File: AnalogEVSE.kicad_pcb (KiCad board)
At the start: 2 copper layers, 84.7 x 66 mm, 72 parts, among them K1 Relay, P1 230V, P2 Relay 2, P3 Relay 1, P4 Pilot, P5 Status LEDs, P6 Rext, P7 Power, Q1 BC337, Q2 BC557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

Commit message: Cleanup
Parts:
- C3: value 220n -> 1u
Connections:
- U5 pad 12: -12V -> Net-(U5-Pad12)
- U5 pad 3: +12V -> Net-(U5-Pad3)
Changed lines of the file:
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@@
     (zones 0)
     (modules 72)
-    (nets 52)
+    (nets 54)
   )
   (page A4)
@@
   (net 50 "Net-(U4-Pad9)")
   (net 51 "Net-(U4-Pad13)")
+  (net 52 "Net-(U5-Pad3)")
+  (net 53 "Net-(U5-Pad12)")
   (net_class Default "This is the default net class."
     (clearance 0.1)
@@
     (add_net "Net-(U4-Pad7)")
     (add_net "Net-(U4-Pad9)")
+    (add_net "Net-(U5-Pad12)")
+    (add_net "Net-(U5-Pad3)")
     (add_net Vcharge)
     (add_net Vconn)
@@
       (effects (font (size 1.016 1.016) (thickness 0.2032)))
     )
-    (fp_text value 220n (at 0 0 180) (layer F.SilkS) hide
+    (fp_text value 1u (at 0 0 180) (layer F.SilkS) hide
       (effects (font (size 1.016 1.016) (thickness 0.2032)))
     )
@@
       (net 38 "Net-(R10-Pad1)"))
     (pad 3 thru_hole oval (at -2.54 3.81 270) (size 1.5 2.286) (drill 0.8) (layers *.Cu *.Mask F.SilkS)
-      (net 1 +12V))
+      (net 52 "Net-(U5-Pad3)"))
     (pad 4 thru_hole oval (at 0 3.81 270) (size 1.5 2.286) (drill 0.8) (layers *.Cu *.Mask F.SilkS)
       (net 24 "Net-(C11-Pad1)"))
@@
       (net 38 "Net-(R10-Pad1)"))
     (pad 12 thru_hole oval (at -2.54 -3.81 270) (size 1.5 2.286) (drill 0.8) (layers *.Cu *.Mask F.SilkS)
-      (net 2 -12V))
+      (net 53 "Net-(U5-Pad12)"))
     (pad 13 thru_hole oval (at -5.08 -3.81 270) (size 1.5 2.286) (drill 0.8) (layers *.Cu *.Mask F.SilkS)
       (net 39 "Net-(R15-Pad1)"))

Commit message: Release 2.0.3
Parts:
- removed the ? at (137.5, 73.3)
- removed the ? at (137.5, 77.7)
- removed the ? at (164.6, 66.9)
- removed the ? at (164.6, 72.0)
- moved D3 1.42 mm to (176.0, 53.5), turned to 0 degrees
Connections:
- K1 pad 8: +12V -> Net-(C6-Pad2)
- K1 pad 9: Net-(C6-Pad2) -> +12V
- U5 pad 12: Net-(U5-Pad12) -> -12V
- U5 pad 3: Net-(U5-Pad3) -> +12V
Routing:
- net +12V: track 285.6 -> 271.3 mm, vias 4 -> 2
- net Net-(D11-Pad2): track 83.7 -> 69.8 mm
- net Net-(D11-Pad1): track 37.2 -> 50.0 mm
- net Net-(D6-Pad1): track 142.1 -> 143.5 mm
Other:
- net class Power: via_dia 1.4 -> 1.6; via_drill 0.6 -> 0.8
- board text added: "www.analogevse.xyz v2.0.3 12/2019"
- board text removed: "www.analogevse.xyz v2.0.0 01/2019"

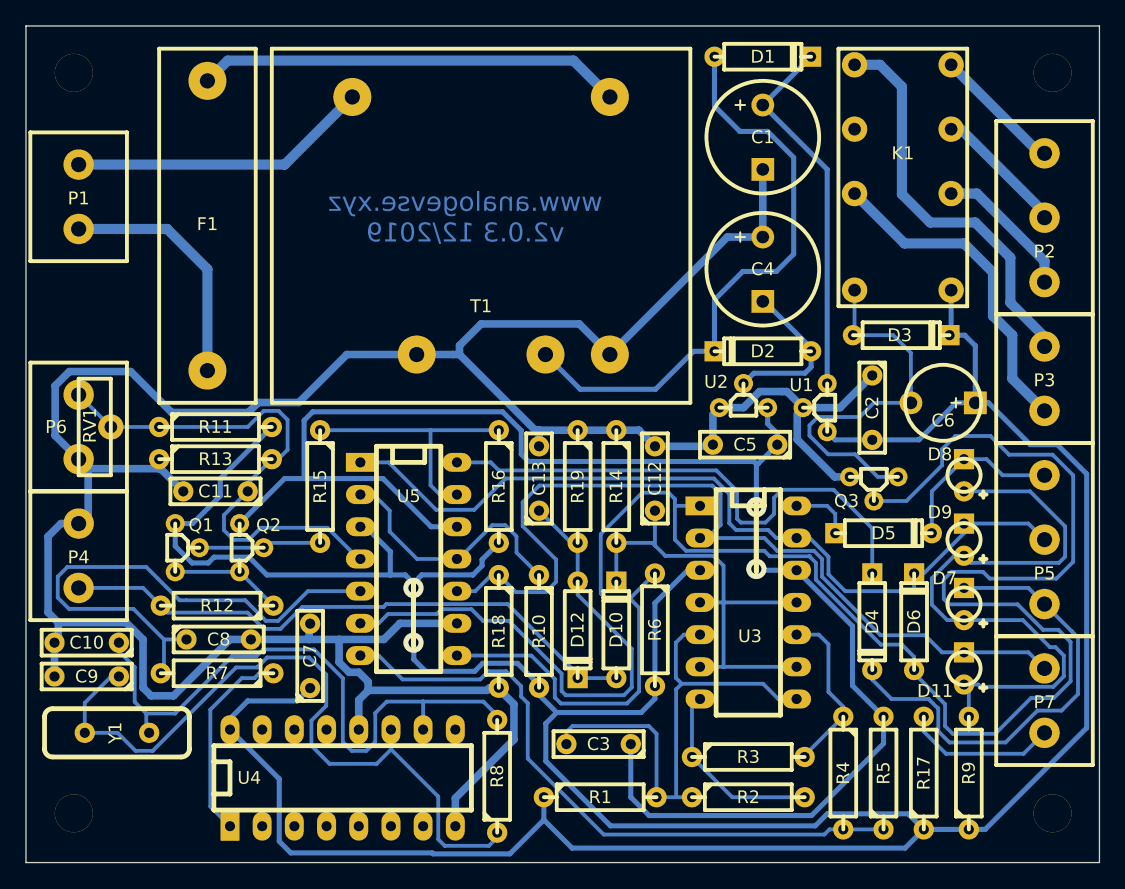
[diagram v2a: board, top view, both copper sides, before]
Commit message: Version 2.0.4 with R20 for proper +12V when idle
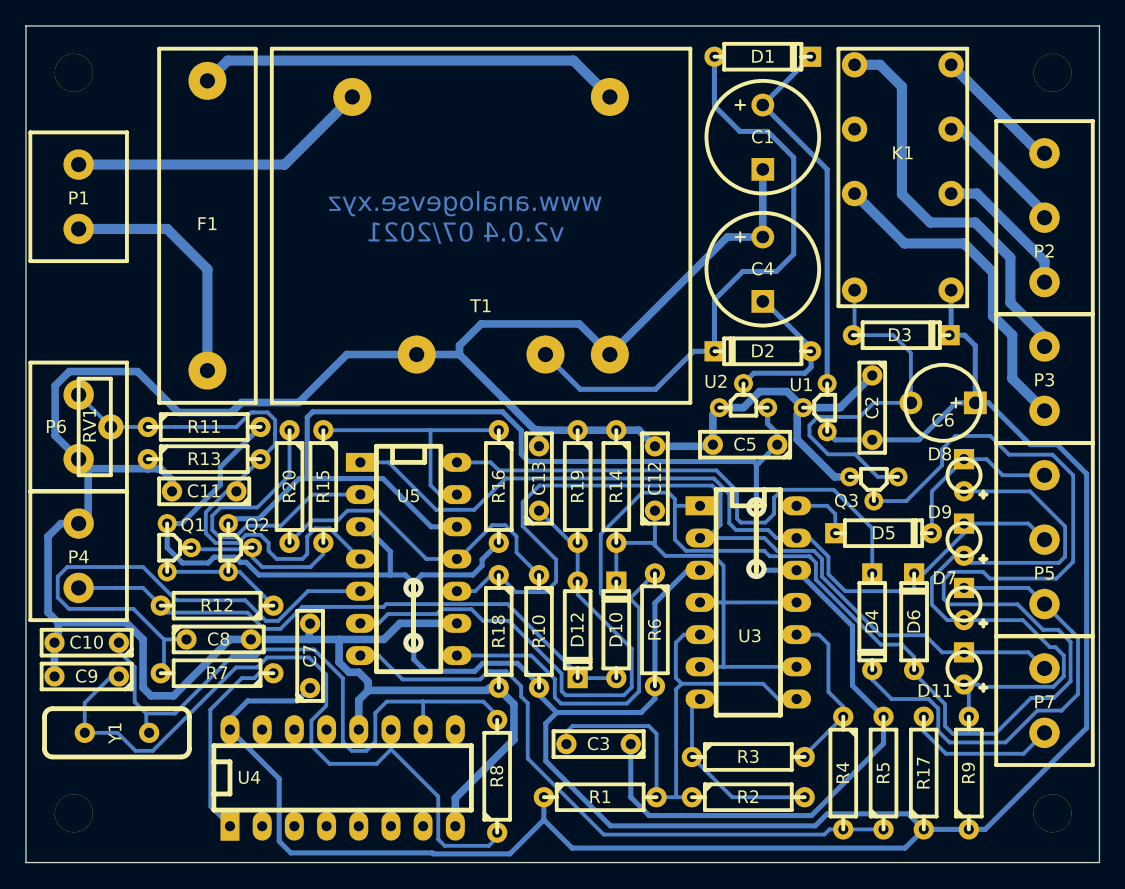
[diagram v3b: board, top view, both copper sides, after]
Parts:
- added R20: 1k, mylib:R3.5, F.Cu at (127.8, 65.4)
- moved C11 0.89 mm to (121.0, 65.8)
- moved Q2 0.89 mm to (123.6, 70.2)
- moved R11 0.89 mm to (121.0, 60.7)
- moved R13 0.89 mm to (121.0, 63.2)
- moved Q1 0.63 mm to (118.7, 70.2)
- moved R15 0.25 mm to (130.4, 65.4)
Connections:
- U5 pad 2: Net-(R10-Pad1) -> Net-(R20-Pad1)
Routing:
- net Net-(R20-Pad1): track 0.00 -> 25.4 mm
- net Net-(R10-Pad1): track 21.3 -> 26.4 mm
- net Net-(C11-Pad1): track 42.3 -> 46.7 mm
- net Net-(Q1-Pad2): track 9.68 -> 12.9 mm
- net Net-(Q1-Pad1): track 8.85 -> 9.49 mm
- net -12V: track 124.4 -> 124.9 mm
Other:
- board text added: "www.analogevse.xyz v2.0.4 07/2021"
- board text removed: "www.analogevse.xyz v2.0.3 12/2019"
